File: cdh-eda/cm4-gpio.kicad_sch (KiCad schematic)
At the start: 20 parts, among them J1 THD-20-R, P1 S04B-PASK-2(LF)(SN), P2 S04B-PASK-2(LF)(SN), U1 ATA6560-GAQW-VAO, U3 MCP2515T-I/SO, U4 74LVC1G07SE-7

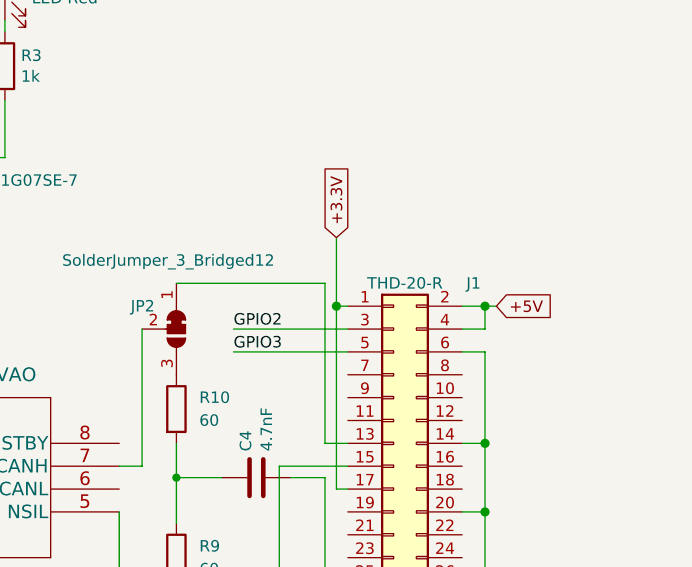
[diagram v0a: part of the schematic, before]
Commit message: v.2 updates
created separate BOMS for JCLPCB and In house purchases
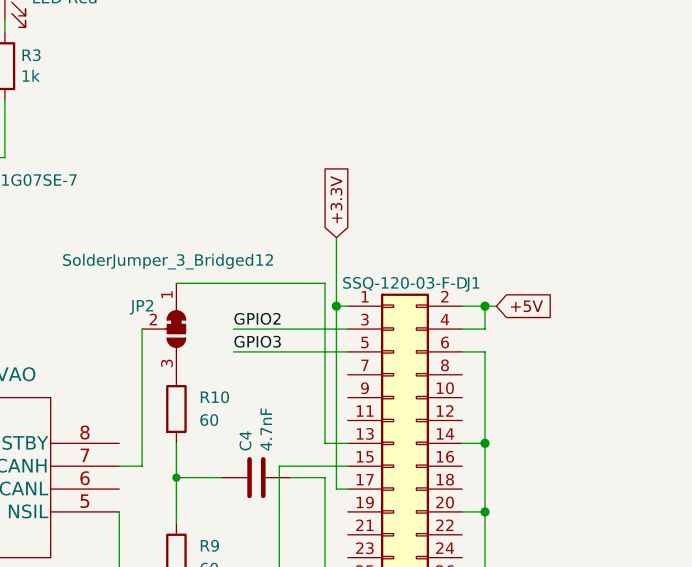
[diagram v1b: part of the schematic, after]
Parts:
- J1: value THD-20-R -> SSQ-120-03-F-D; Field4 Toby -> (none); Field5 THD-20-R -> (none); Field6 THD-20-R -> (none); Field7 Toby -> (none); Field8 UCON00511 -> (none)
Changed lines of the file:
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@@
     (in_bom yes) (on_board yes)
     (property "Reference" "J1" (id 0) (at 271.78 53.34 0))
-    (property "Value" "THD-20-R" (id 1) (at 264.16 53.34 0))
+    (property "Value" "SSQ-120-03-F-D" (id 1) (at 264.16 53.34 0))
     (property "Footprint" "Connector_PinHeader_2.54mm:PinHeader_2x20_P2.54mm_Vertical" (id 2) (at 262.89 78.74 0)
       (effects (font (size 1.27 1.27)) hide)
     )
-    (property "Datasheet" "https://www.toby.co.uk/uploads/publications/1673.pdf" (id 3) (at 262.89 78.74 0)
+    (property "Datasheet" "" (id 3) (at 262.89 78.74 0)
       (effects (font (size 1.27 1.27)) hide)
     )
-    (property "Field4" "Toby" (id 4) (at 262.89 78.74 0)
+    (property "Field4" "" (id 4) (at 262.89 78.74 0)
       (effects (font (size 1.27 1.27)) hide)
     )
-    (property "Field5" "THD-20-R" (id 5) (at 262.89 78.74 0)
+    (property "Field5" "" (id 5) (at 262.89 78.74 0)
       (effects (font (size 1.27 1.27)) hide)
     )
-    (property "Field6" "THD-20-R" (id 6) (at 262.89 78.74 0)
+    (property "Field6" "" (id 6) (at 262.89 78.74 0)
       (effects (font (size 1.27 1.27)) hide)
     )
-    (property "Field7" "Toby" (id 7) (at 262.89 78.74 0)
+    (property "Field7" "" (id 7) (at 262.89 78.74 0)
       (effects (font (size 1.27 1.27)) hide)
     )
-    (property "Field8" "UCON00511" (id 8) (at 262.89 78.74 0)
+    (property "Field8" "" (id 8) (at 262.89 78.74 0)
       (effects (font (size 1.27 1.27)) hide)
     )
